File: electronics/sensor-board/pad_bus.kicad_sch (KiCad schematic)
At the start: 7 parts, among them J13 Conn_02x04_Odd_Even, J14 Conn_02x04_Odd_Even, U10 TJA1042T-3

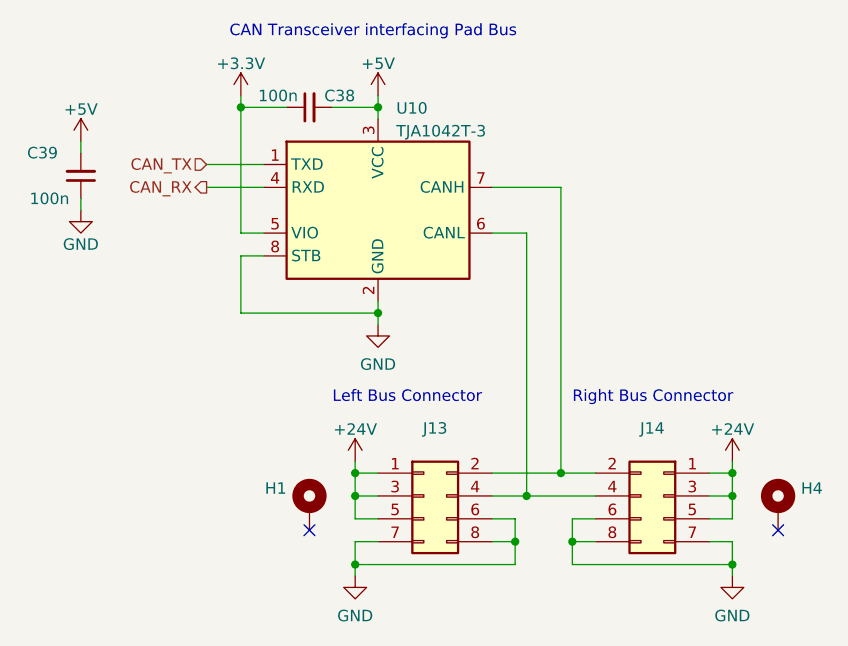
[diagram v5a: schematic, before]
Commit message: Update reference designators
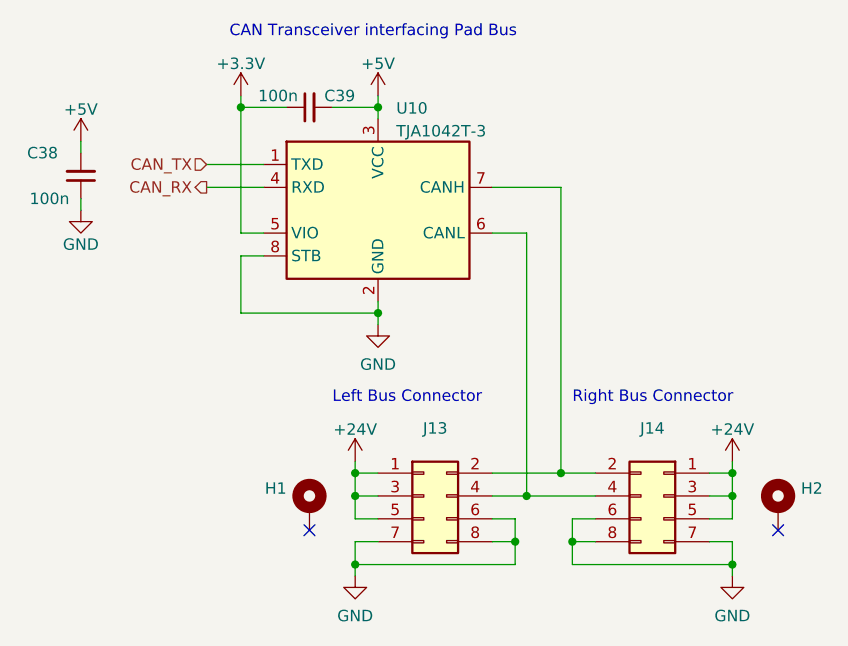
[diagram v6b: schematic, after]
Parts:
- renumbered C39 to C38, C38 to C39, H4 to H2
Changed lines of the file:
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@@
   (symbol (lib_id "power:+24V") (at 54.61 67.31 0) (unit 1)
     (in_bom yes) (on_board yes) (fields_autoplaced)
-    (property "Reference" "#PWR0146" (id 0) (at 54.61 71.12 0)
+    (property "Reference" "#PWR085" (id 0) (at 54.61 71.12 0)
       (effects (font (size 1.27 1.27)) hide)
     )
@@
   (symbol (lib_id "Mechanical:MountingHole_Pad") (at 101.6 72.39 0) (unit 1)
     (in_bom yes) (on_board yes) (fields_autoplaced)
-    (property "Reference" "H4" (id 0) (at 104.14 70.2853 0)
+    (property "Reference" "H2" (id 0) (at 104.14 70.2853 0)
       (effects (font (size 1.27 1.27)) (justify left))
     )
@@
   (symbol (lib_id "power:GND") (at 24.13 39.37 0) (unit 1)
     (in_bom yes) (on_board yes)
-    (property "Reference" "#PWR096" (id 0) (at 24.13 45.72 0)
+    (property "Reference" "#PWR083" (id 0) (at 24.13 45.72 0)
       (effects (font (size 1.27 1.27)) hide)
     )
@@
   (symbol (lib_id "Device:C_Small") (at 24.13 35.56 180) (unit 1)
     (in_bom yes) (on_board yes)
-    (property "Reference" "C39" (id 0) (at 21.59 33.02 0)
+    (property "Reference" "C38" (id 0) (at 21.59 33.02 0)
       (effects (font (size 1.27 1.27)) (justify left))
     )
@@
   (symbol (lib_id "power:GND") (at 57.15 52.07 0) (unit 1)
     (in_bom yes) (on_board yes)
-    (property "Reference" "#PWR094" (id 0) (at 57.15 58.42 0)
+    (property "Reference" "#PWR088" (id 0) (at 57.15 58.42 0)
       (effects (font (size 1.27 1.27)) hide)
     )
@@
   (symbol (lib_id "power:+5V") (at 24.13 31.75 0) (unit 1)
     (in_bom yes) (on_board yes) (fields_autoplaced)
-    (property "Reference" "#PWR095" (id 0) (at 24.13 35.56 0)
+    (property "Reference" "#PWR082" (id 0) (at 24.13 35.56 0)
       (effects (font (size 1.27 1.27)) hide)
     )
@@
   (symbol (lib_id "power:GND") (at 96.52 80.01 0) (mirror y) (unit 1)
     (in_bom yes) (on_board yes) (fields_autoplaced)
-    (property "Reference" "#PWR0106" (id 0) (at 96.52 86.36 0)
+    (property "Reference" "#PWR090" (id 0) (at 96.52 86.36 0)
       (effects (font (size 1.27 1.27)) hide)
     )
@@
   (symbol (lib_id "power:GND") (at 54.61 80.01 0) (unit 1)
     (in_bom yes) (on_board yes) (fields_autoplaced)
-    (property "Reference" "#PWR0144" (id 0) (at 54.61 86.36 0)
+    (property "Reference" "#PWR086" (id 0) (at 54.61 86.36 0)
       (effects (font (size 1.27 1.27)) hide)
     )
@@
   (symbol (lib_id "power:+5V") (at 57.15 26.67 0) (unit 1)
     (in_bom yes) (on_board yes) (fields_autoplaced)
-    (property "Reference" "#PWR093" (id 0) (at 57.15 30.48 0)
+    (property "Reference" "#PWR087" (id 0) (at 57.15 30.48 0)
       (effects (font (size 1.27 1.27)) hide)
     )
@@
   (symbol (lib_id "power:+3.3V") (at 41.91 26.67 0) (unit 1)
     (in_bom yes) (on_board yes) (fields_autoplaced)
-    (property "Reference" "#PWR092" (id 0) (at 41.91 30.48 0)
+    (property "Reference" "#PWR084" (id 0) (at 41.91 30.48 0)
       (effects (font (size 1.27 1.27)) hide)
     )
@@
   (symbol (lib_id "Device:C_Small") (at 49.53 27.94 90) (unit 1)
     (in_bom yes) (on_board yes)
-    (property "Reference" "C38" (id 0) (at 54.61 26.67 90)
+    (property "Reference" "C39" (id 0) (at 54.61 26.67 90)
       (effects (font (size 1.27 1.27)) (justify left))
     )
@@
   (symbol (lib_id "power:+24V") (at 96.52 67.31 0) (mirror y) (unit 1)
     (in_bom yes) (on_board yes) (fields_autoplaced)
-    (property "Reference" "#PWR0132" (id 0) (at 96.52 71.12 0)
-      (effects (font (size 1.27 1.27)) hide)
-    )
+    (property "Reference" "#PWR089" (id 0) (at 96.52 71.12 0)
+      (effects (font (size 1.27 1.27)) hide)
+    )

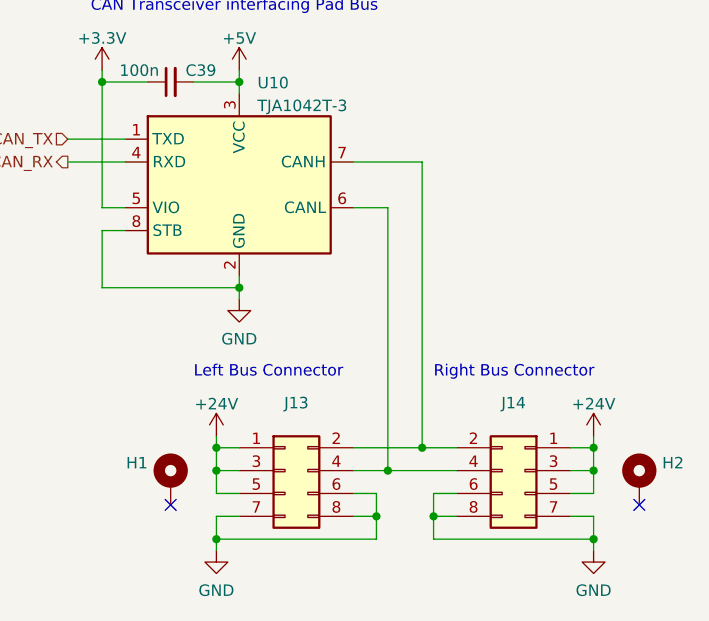
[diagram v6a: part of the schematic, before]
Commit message: Switch to G4, preliminary signal layout
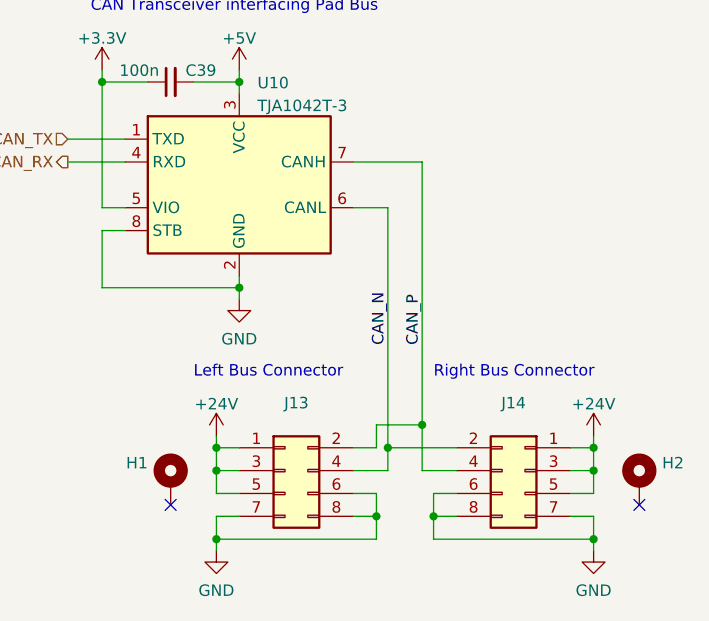
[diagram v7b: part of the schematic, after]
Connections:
- net CAN_P: now reaches J13.2 (Pin_2), U10.7 (CANH)
- net CAN_P: now also J14.4 (Pin_4); no longer J14.2 (Pin_2)
- net CAN_N: now reaches J13.4 (Pin_4), U10.6 (CANL)
- net CAN_N: now also J14.2 (Pin_2); no longer J14.4 (Pin_4)
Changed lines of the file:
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@@
 (kicad_sch (version 20211123) (generator eeschema)
   (paper "A4")
+  (junction (at 73.66 68.58) (diameter 0) (color 0 0 0 0)
+  )
   (junction (at 54.61 68.58) (diameter 0) (color 0 0 0 0)
   )
   (junction (at 57.15 27.94) (diameter 0) (color 0 0 0 0)
   )
+  (junction (at 77.47 66.04) (diameter 0) (color 0 0 0 0)
+  )
   (junction (at 96.52 78.74) (diameter 0) (color 0 0 0 0)
   )
@@
   (junction (at 96.52 68.58) (diameter 0) (color 0 0 0 0)
   )
-  (junction (at 77.47 68.58) (diameter 0) (color 0 0 0 0)
-  )
   (junction (at 72.39 76.2) (diameter 0) (color 0 0 0 0)
-  )
-  (junction (at 73.66 71.12) (diameter 0) (color 0 0 0 0)
   )
   (no_connect (at 49.53 74.93))
@@
     (stroke (width 0) (type default) (color 0 0 0 0))
   )
+  (wire (pts (xy 72.39 68.58) (xy 69.85 68.58))
+    (stroke (width 0) (type default) (color 0 0 0 0))
+  )
+  (wire (pts (xy 77.47 66.04) (xy 77.47 71.12))
+    (stroke (width 0) (type default) (color 0 0 0 0))
+  )
   (wire (pts (xy 54.61 68.58) (xy 54.61 67.31))
     (stroke (width 0) (type default) (color 0 0 0 0))
@@
     (stroke (width 0) (type default) (color 0 0 0 0))
   )
+  (wire (pts (xy 73.66 71.12) (xy 69.85 71.12))
+    (stroke (width 0) (type default) (color 0 0 0 0))
+  )
   (wire (pts (xy 41.91 44.45) (xy 41.91 50.8))
     (stroke (width 0) (type default) (color 0 0 0 0))
   )
+  (wire (pts (xy 77.47 66.04) (xy 72.39 66.04))
+    (stroke (width 0) (type default) (color 0 0 0 0))
+  )
   (wire (pts (xy 57.15 50.8) (xy 57.15 49.53))
     (stroke (width 0) (type default) (color 0 0 0 0))
@@
     (stroke (width 0) (type default) (color 0 0 0 0))
   )
-  (wire (pts (xy 73.66 41.91) (xy 73.66 71.12))
-    (stroke (width 0) (type default) (color 0 0 0 0))
-  )
-  (wire (pts (xy 73.66 71.12) (xy 81.28 71.12))
-    (stroke (width 0) (type default) (color 0 0 0 0))
-  )
   (wire (pts (xy 69.85 41.91) (xy 73.66 41.91))
     (stroke (width 0) (type default) (color 0 0 0 0))
   )
-  (wire (pts (xy 77.47 68.58) (xy 81.28 68.58))
-    (stroke (width 0) (type default) (color 0 0 0 0))
-  )
   (wire (pts (xy 93.98 71.12) (xy 96.52 71.12))
     (stroke (width 0) (type default) (color 0 0 0 0))
@@
     (stroke (width 0) (type default) (color 0 0 0 0))
   )
+  (wire (pts (xy 73.66 68.58) (xy 73.66 71.12))
+    (stroke (width 0) (type default) (color 0 0 0 0))
+  )
   (wire (pts (xy 57.15 71.12) (xy 54.61 71.12))
     (stroke (width 0) (type default) (color 0 0 0 0))
@@
     (stroke (width 0) (type default) (color 0 0 0 0))
   )
-  (wire (pts (xy 69.85 68.58) (xy 77.47 68.58))
-    (stroke (width 0) (type default) (color 0 0 0 0))
-  )
   (wire (pts (xy 57.15 27.94) (xy 57.15 29.21))
     (stroke (width 0) (type default) (color 0 0 0 0))
   )
+  (wire (pts (xy 73.66 68.58) (xy 81.28 68.58))
+    (stroke (width 0) (type default) (color 0 0 0 0))
+  )
+  (wire (pts (xy 72.39 66.04) (xy 72.39 68.58))
+    (stroke (width 0) (type default) (color 0 0 0 0))
+  )
   (wire (pts (xy 54.61 71.12) (xy 54.61 68.58))
     (stroke (width 0) (type default) (color 0 0 0 0))
@@
     (stroke (width 0) (type default) (color 0 0 0 0))
   )
-  (wire (pts (xy 77.47 68.58) (xy 77.47 36.83))
+  (wire (pts (xy 77.47 36.83) (xy 77.47 66.04))
+    (stroke (width 0) (type default) (color 0 0 0 0))
+  )
+  (wire (pts (xy 73.66 41.91) (xy 73.66 68.58))
     (stroke (width 0) (type default) (color 0 0 0 0))
   )
@@
     (stroke (width 0) (type default) (color 0 0 0 0))
   )
-  (wire (pts (xy 69.85 71.12) (xy 73.66 71.12))
-    (stroke (width 0) (type default) (color 0 0 0 0))
-  )
   (wire (pts (xy 41.91 27.94) (xy 46.99 27.94))
     (stroke (width 0) (type default) (color 0 0 0 0))
@@
     (stroke (width 0) (type default) (color 0 0 0 0))
   )
+  (wire (pts (xy 77.47 71.12) (xy 81.28 71.12))
+    (stroke (width 0) (type default) (color 0 0 0 0))
+  )
   (wire (pts (xy 57.15 26.67) (xy 57.15 27.94))
     (stroke (width 0) (type default) (color 0 0 0 0))
@@
     (effects (font (size 1.27 1.27)) (justify left bottom))
   )
+  (label "CAN_P" (at 77.47 57.15 90)
+    (effects (font (size 1.27 1.27)) (justify left bottom))
+  )
+  (label "CAN_N" (at 73.66 57.15 90)
+    (effects (font (size 1.27 1.27)) (justify left bottom))
+  )
